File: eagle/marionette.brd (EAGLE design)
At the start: 139.7 x 76.2 mm, 227 parts, among them J17 MA02-1, J18 MA02-1, J19 MA02-1, J2 SWD, J20 MA02-1, J22 ZX62D-B-5P8, J6 MA03-2W, J8 MA04-2W, Q1 BSS84, U1 STM32F407, U10 LVM344, U12 AT24C04D, U13 CON_HIROSE_DM3D(MICROSD), U14 USB3320, U2 NCP705, U3 XCL206B, U4 AAT3221, U5 MAX3051ESA, U6 DAC124S085CIMM, U7 LVM344, U8 LVM344, U9 LVM344, X1 ABSO7, X2 NX3225SA

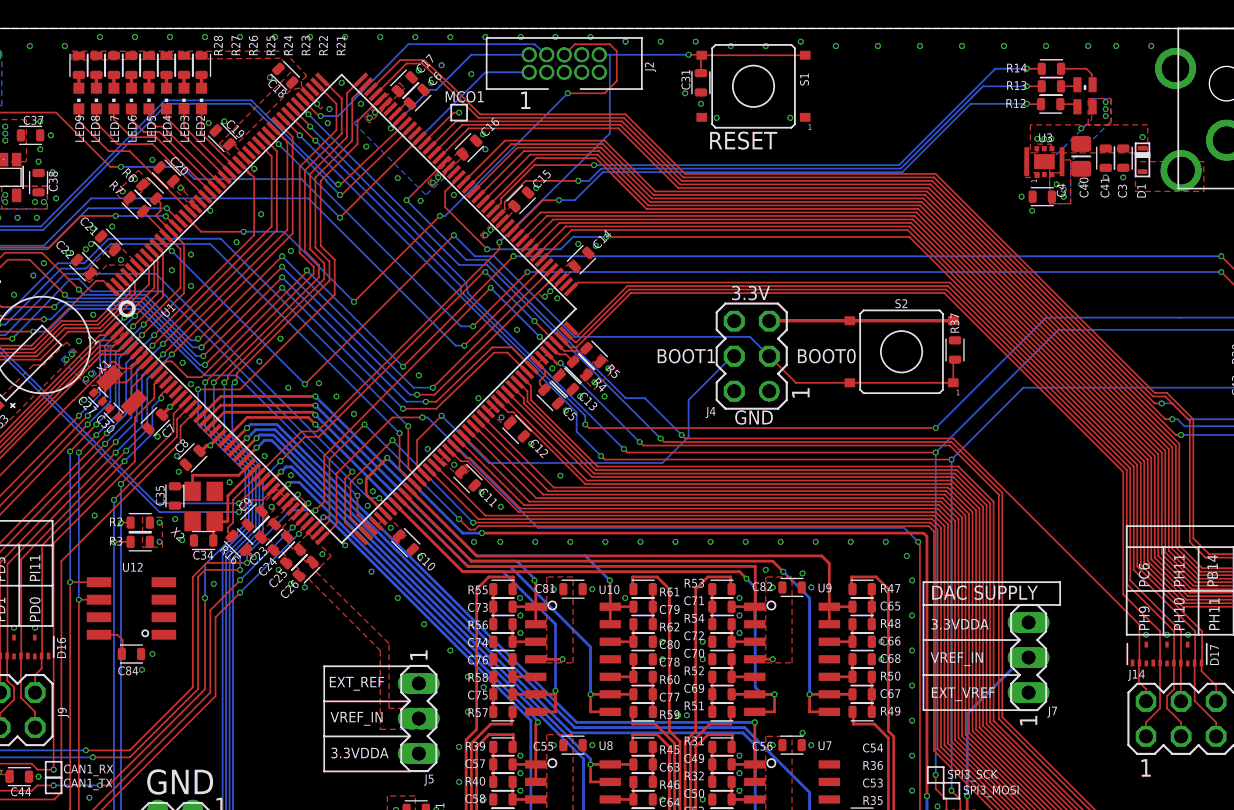
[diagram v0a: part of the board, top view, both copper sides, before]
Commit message: Added new 3.3V SPS and related LC components Changed Vin header to DAC from 3pin to 2pin
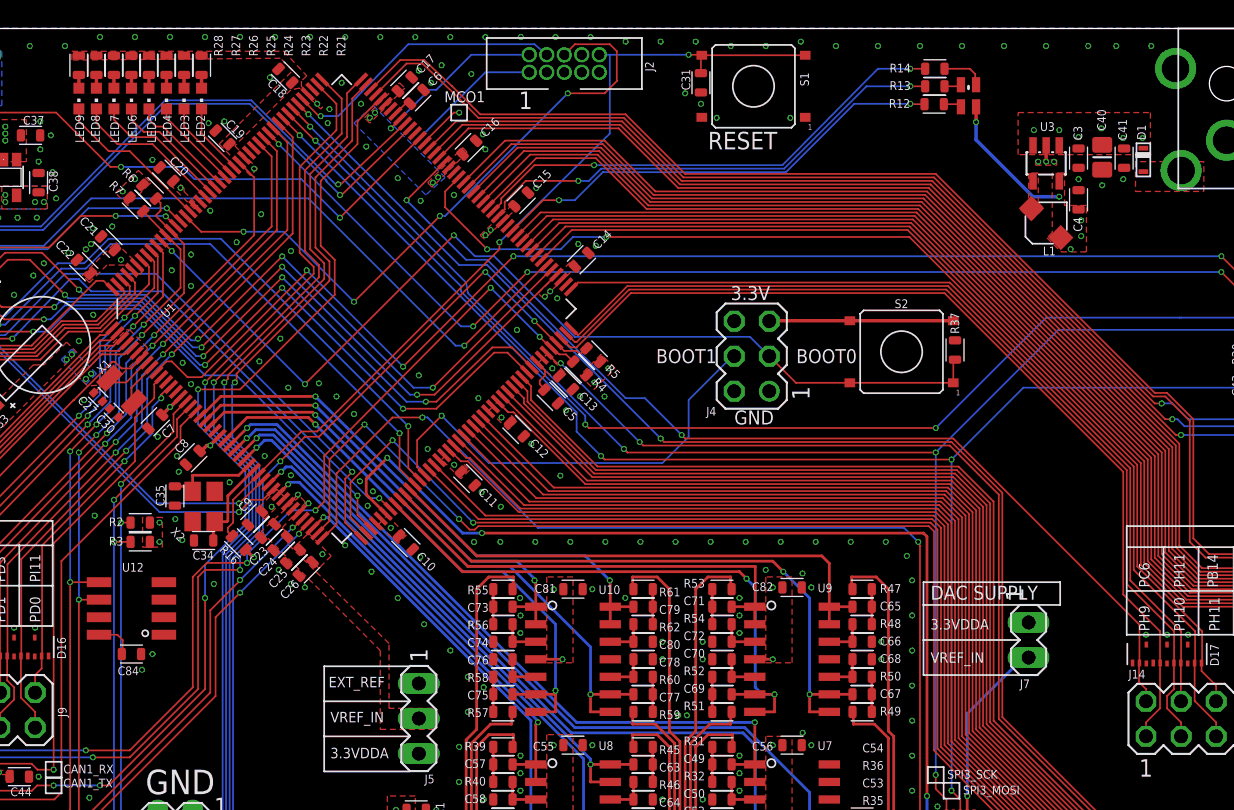
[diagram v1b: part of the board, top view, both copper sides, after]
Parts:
- added L1: 2.2uH, rcl_custom:CDRH2D14
- C1, C2, C23, C25, C37, C38, C41, C46: value 1uF, 10V -> 1uF
- C10, C12, C13, C14, C15, C16, C17, C18, C19, C20, C21, C24, C26, C31, C7, C8, C9: value 100nF, 10V -> .1uF
- C11: value 100nF, 10V -> .1uf
- C22: value 4.7uF, 10v -> 4.7uF
- C3: value 4.7uF, 10V -> 4.7uF
- C33: value EDLC -> 220mF
- C39, C4, C40, C45: value 10uF, 10V -> 10uF
- C47: value 0.1uF, 10V Low ESR -> 0.1uF
- C5, C6: value 2.2uF, 10V -> 2.2uF
- C55, C56, C81, C82: value (none) -> 1uF
- J7: value (none) -> MA02-1; device MA_HEADER:MA03-1 -> MA_HEADER:MA02-1
- U3: value XCL206B -> LM3671; device XCL206B:56-BCPGA -> LM3671:SOT23-5L
- moved LED1 8.45 mm to (97.2, 71.3)
- moved R13 8.45 mm to (94.8, 72.0)
- moved R14 8.45 mm to (94.8, 73.3)
- moved R12 8.45 mm to (94.8, 70.7)
- moved C3 3.24 mm to (105.2, 66.8)
- moved C4 2.64 mm to (105.2, 63.8), turned to 90 degrees
- moved C40 1.53 mm to (106.9, 66.9)
- moved C41 1.33 mm to (108.5, 66.8)
- moved J7 1.27 mm to (101.6, 31.9), turned to 270 degrees
- moved U3 0.18 mm to (102.9, 66.4), turned to 180 degrees
- moved D1 0.06 mm to (109.9, 66.7)
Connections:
- removed net N$5: U3.1, U3.7
- new net N$41: L1.2, U3.4
- net +3.3VDDA: now also J7.1; no longer J7.3
- net 3.3VDD: now also L1.1, U3.5; no longer U3.3, U3.8
- net GND: no longer U3.5, U3.9
- net VCC: now also U3.1, U3.3; no longer U3.4, U3.6
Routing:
- net 3.3VDD: track 32.7 -> 42.8 mm, vias 46 -> 45
- net PD13: track 42.2 -> 33.7 mm
- net PD14: track 43.8 -> 35.4 mm
- net PD15: track 44.2 -> 35.8 mm
- net GND: track 2.46 -> 3.63 mm, vias 414 -> 415
- added copper zone on layer 1, net N$41
- removed copper zone on layer 1, net N$5
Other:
- board text removed: "EXT_VREF"

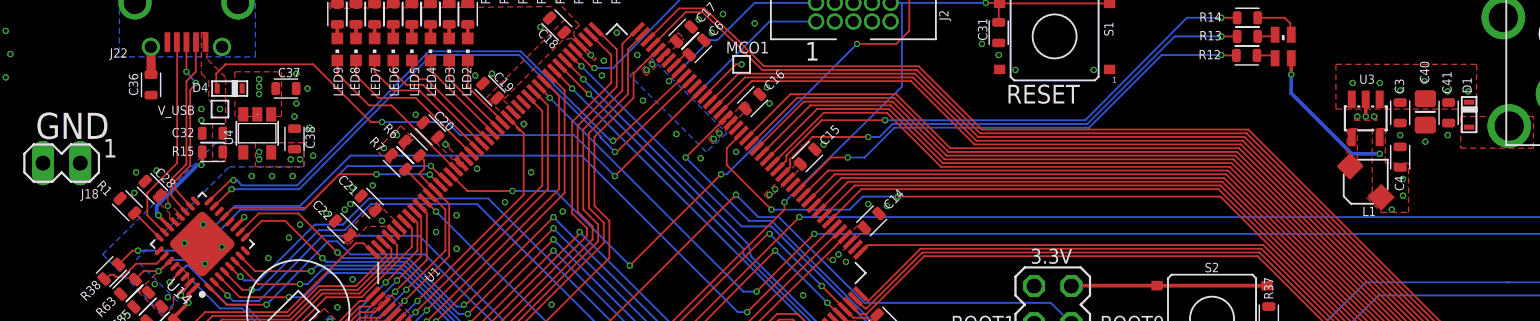
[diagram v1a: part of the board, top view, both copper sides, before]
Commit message: added 0805 10uF cap to 3.3sps.
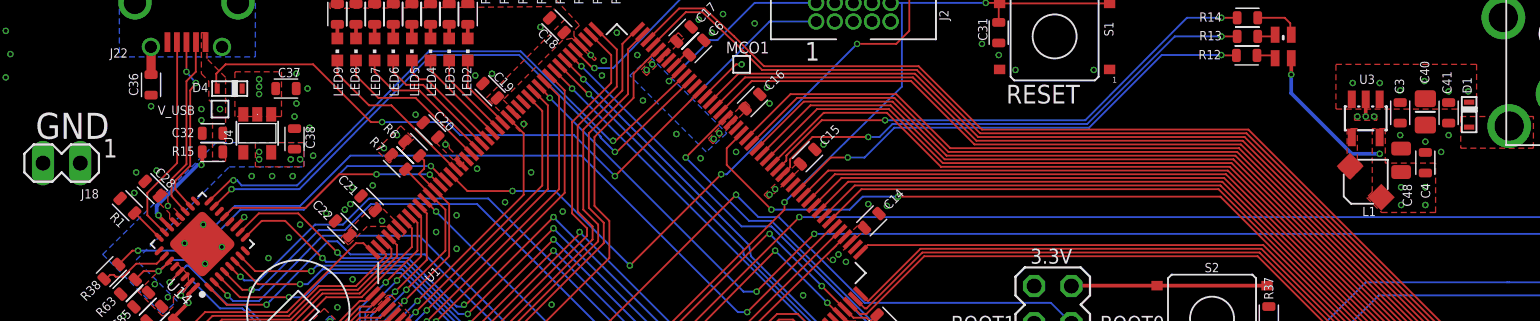
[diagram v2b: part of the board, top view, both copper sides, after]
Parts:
- added C48: 10uf, rcl_custom:.0805-C-NOSILK
- C4: value 10uF -> 1uf
- moved C4 1.76 mm to (106.9, 63.4)
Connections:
- net 3.3VDD: now also C48.1
- net GND: now also C48.2
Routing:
- net GND: vias 415 -> 417
- net 3.3VDD: vias 45 -> 46
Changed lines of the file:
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@@
 <attribute name="NAME" x="93.345" y="16.129" size="0.3" layer="33" ratio="15" rot="R270" align="center"/>
 </element>
-<element name="C4" library="rcl_custom" package=".0603-C" value="10uF" x="105.2195" y="63.7794" smashed="yes" rot="R90">
-<attribute name="NAME" x="105.4855" y="61.4713" size="0.635" layer="25" font="vector" ratio="20" rot="R90"/>
-<attribute name="NAME" x="105.2195" y="63.7794" size="0.3" layer="33" ratio="15" rot="R90" align="center"/>
+<element name="C4" library="rcl_custom" package=".0603-C" value="1uf" x="106.934" y="63.3984" smashed="yes" rot="R90">
+<attribute name="NAME" x="107.2635" y="60.9633" size="0.635" layer="25" font="vector" ratio="20" rot="R90"/>
+<attribute name="NAME" x="106.934" y="63.3984" size="0.3" layer="33" ratio="15" rot="R90" align="center"/>
 </element>
 <element name="C40" library="rcl_custom" package=".0805-B" value="10uF" x="106.934" y="66.8655" smashed="yes" rot="R270">
@@
 </element>
 <element name="R1" library="rcl_custom" package=".0603-C" value="8.06k" x="18.452196875" y="60.46740625" smashed="yes" rot="R135">
-<attribute name="NAME" x="17.497640625" y="61.514875" size="0.635" layer="25" font="vector" ratio="20" rot="R135"/>
+<attribute name="NAME" x="18.386640625" y="59.355875" size="0.635" layer="25" font="vector" ratio="20" rot="R135"/>
 <attribute name="NAME" x="18.452196875" y="60.46740625" size="0.3" layer="33" ratio="15" rot="R135" align="center"/>
 </element>
@@
 <attribute name="VALUE" x="98.679" y="34.417" size="1.27" layer="27" ratio="10" rot="R270"/>
 </element>
+<element name="C48" library="rcl_custom" package=".0805-C-NOSILK" value="10uf" x="105.283" y="63.5635" smashed="yes" rot="R90">
+<attribute name="NAME" x="106.0205" y="60.4085" size="0.635" layer="25" font="vector" ratio="20" rot="R90"/>
+<attribute name="VALUE" x="106.933" y="62.3135" size="0.8" layer="27" font="vector" ratio="15" rot="R90"/>
+<attribute name="NAME" x="105.283" y="63.5635" size="0.4" layer="33" ratio="15" rot="R90" align="center"/>
+</element>
 </elements>
 <signals>
@@
 <contactref element="U3" pad="2"/>
 <contactref element="C3" pad="2"/>
-<contactref element="C4" pad="2"/>
 <via x="103.4415" y="66.548" extent="1-16" drill="0.254"/>
 <via x="102.87" y="66.548" extent="1-16" drill="0.254"/>
@@
 <via x="105.2195" y="65.278" extent="1-16" drill="0.254"/>
 <via x="106.934" y="64.8335" extent="1-16" drill="0.254"/>
-<via x="108.458" y="65.278" extent="1-16" drill="0.254"/>
+<via x="108.5215" y="65.278" extent="1-16" drill="0.254"/>
 <polygon width="0.127" layer="1" isolate="0.2032" thermals="no" rank="2">
 <vertex x="103.632" y="66.675"/>
@@
 </polygon>
 <wire x1="102.87" y1="67.721" x2="102.87" y2="66.548" width="0.254" layer="1"/>
+<via x="20.066" y="67.2465" extent="1-16" drill="0.254"/>
+<contactref element="C48" pad="2"/>
+<contactref element="C4" pad="2"/>
+<via x="108.0135" y="64.135" extent="1-16" drill="0.254"/>
 <wire x1="22.352" y1="57.912" x2="23.553984375" y2="57.8530125" width="0" layer="19" extent="1-1"/>
 </signal>
@@
 <via x="103.8225" y="68.834" extent="1-16" drill="0.254"/>
 <via x="106.8705" y="68.961" extent="1-16" drill="0.254"/>
-<via x="108.458" y="68.2625" extent="1-16" drill="0.254"/>
+<via x="108.5215" y="68.2625" extent="1-16" drill="0.254"/>
 <via x="109.855" y="68.2625" extent="1-16" drill="0.254"/>
 </signal>
@@
 <contactref element="C4" pad="1"/>
 <polygon width="0.127" layer="1" isolate="0.2032" thermals="no">
-<vertex x="104.0765" y="65.7225"/>
+<vertex x="104.2035" y="65.7225"/>
 <vertex x="103.3145" y="65.7225"/>
-<vertex x="103.3145" y="61.468"/>
 <vertex x="103.3145" y="61.4045"/>
 <vertex x="102.9335" y="61.0235"/>
 <vertex x="103.9495" y="60.0075"/>
-<vertex x="105.791" y="60.0075"/>
-<vertex x="105.791" y="63.373"/>
+<vertex x="107.6325" y="60.0075"/>
+<vertex x="107.6325" y="63.373"/>
 <vertex x="104.2035" y="63.373"/>
-<vertex x="104.2035" y="65.7225"/>
 </polygon>
-<via x="104.648" y="60.198" extent="1-16" drill="0.254"/>
-<via x="105.41" y="61.1505" extent="1-16" drill="0.254"/>
-<via x="105.41" y="62.2935" extent="1-16" drill="0.254"/>
+<via x="105.283" y="60.5155" extent="1-16" drill="0.254"/>
+<via x="106.934" y="61.722" extent="1-16" drill="0.254"/>
+<via x="105.283" y="61.722" extent="1-16" drill="0.254"/>
 <via x="97.79" y="69.4055" extent="1-16" drill="0.254"/>
 <via x="103.8225" y="64.008" extent="1-16" drill="0.254"/>
@@
 <wire x1="97.7939" y1="70.5232" x2="97.7939" y2="69.4094" width="0.254" layer="1"/>
 <wire x1="97.7939" y1="69.4094" x2="97.79" y2="69.4055" width="0.254" layer="1"/>
+<contactref element="C48" pad="1"/>
+<via x="106.934" y="60.5155" extent="1-16" drill="0.254"/>
 </signal>
 <signal name="PD6">

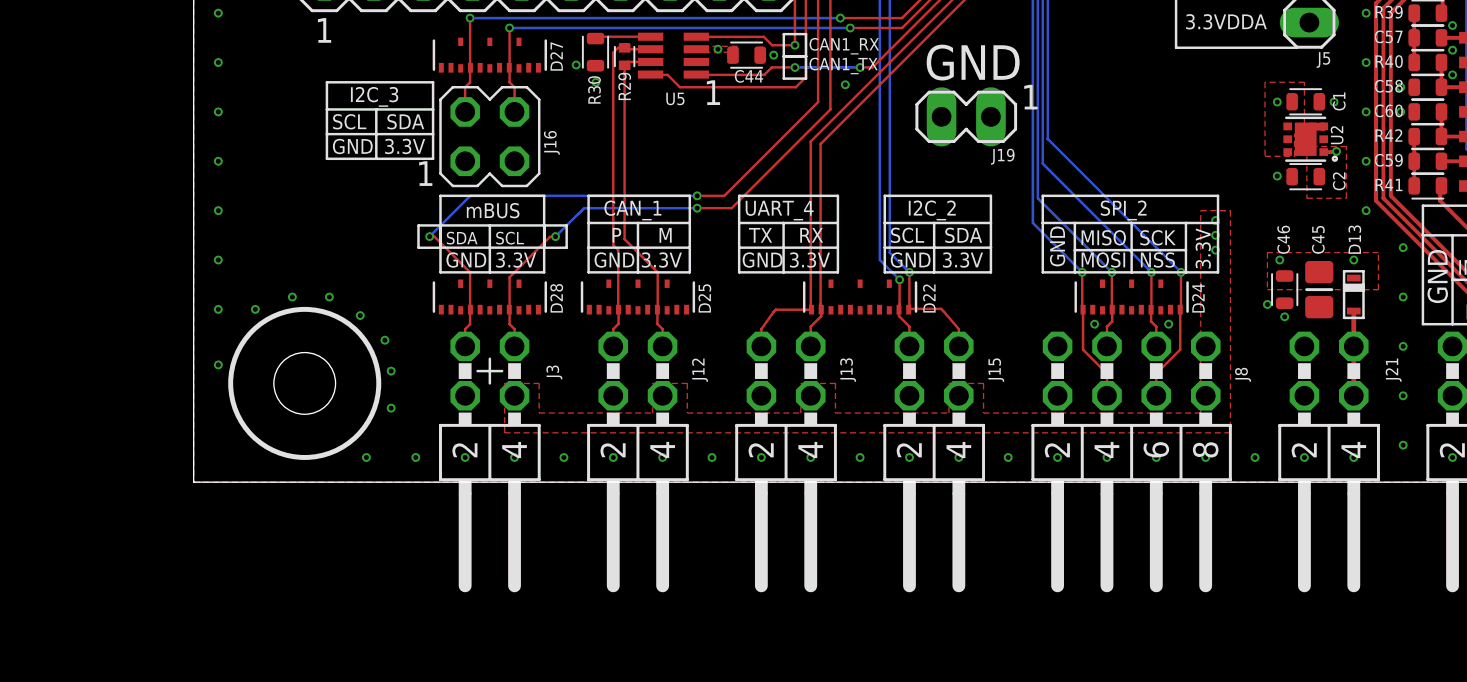
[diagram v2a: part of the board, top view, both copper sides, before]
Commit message: Added new 1.8V/3.3V LDO and associated bypass caps to schematic
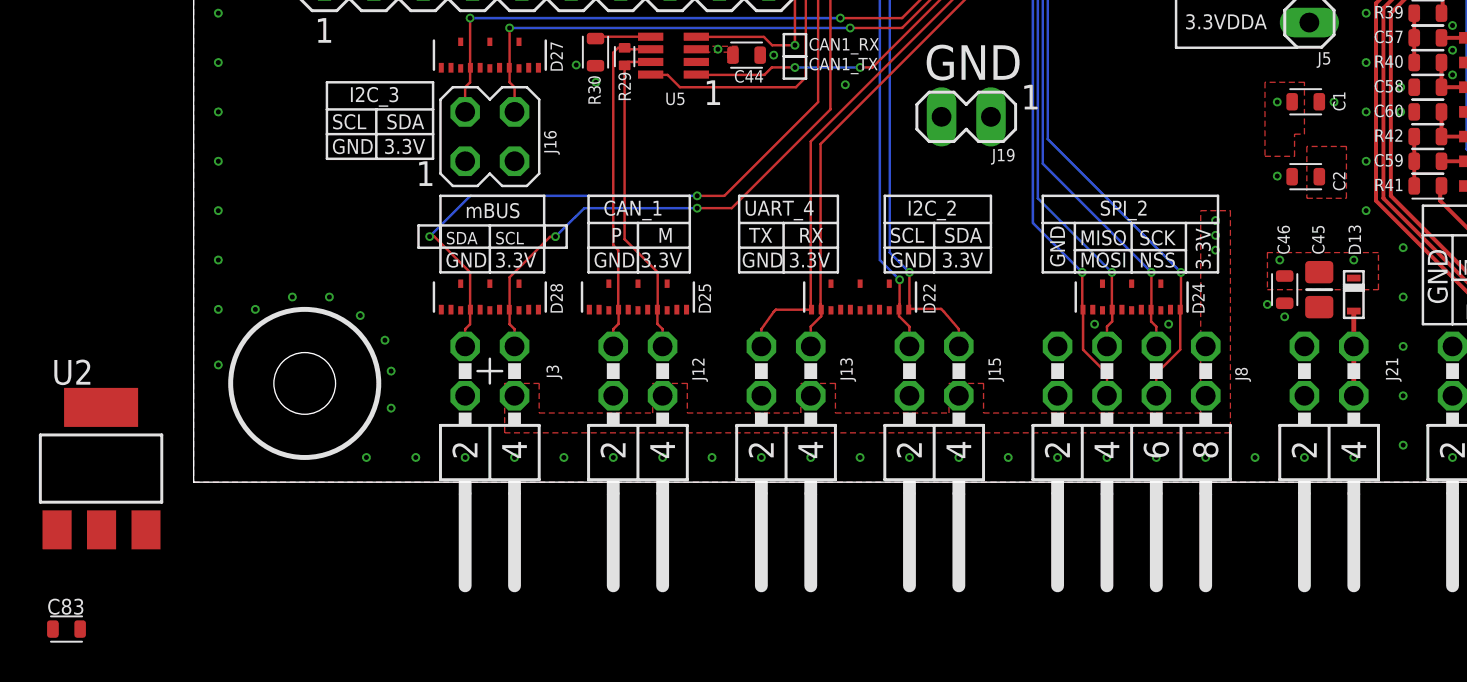
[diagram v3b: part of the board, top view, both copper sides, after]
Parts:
- added C83: 0.1uF, rcl_custom:.0603-C
- C38: value 1uF -> 2.2uF
- U2: value NCP705 -> TC1262; device NCP705:WDFN6 -> TC1262:SOT223
- U4: value AAT3221 -> LK112; device AAT3221:SOT23-5 -> LK112:SOT23-5
- moved U2 64.3 mm to (-4.76, 0.70), turned to 0 degrees
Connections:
- new net N$5: C83.1, U4.3
- net +1.8V: now also U4.4; no longer U4.5
- net +3.3VDDA: now also U2.3; no longer U2.1
- net 3.3VDD: now also C1.1, C37.1, U2.1, U4.1, U4.5
- net GND: now also C83.2, U2.2, U2.4; no longer U2.3, U2.GND
- net VCC: no longer C1.1, C37.1, U2.4, U2.6, U4.1, U4.3
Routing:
- net GND: track 3.63 -> 2.17 mm
- net +3.3VDDA: track 7.35 -> 6.67 mm, vias 13 -> 12

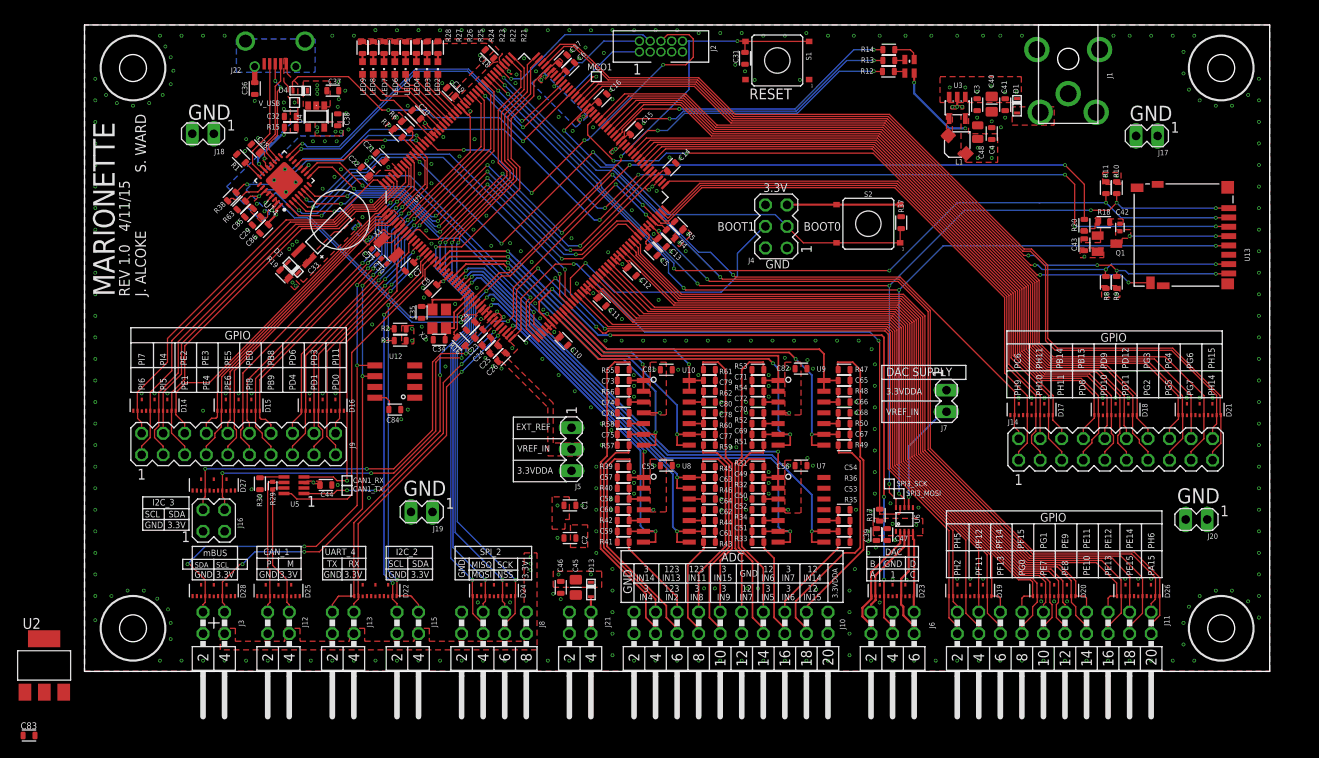
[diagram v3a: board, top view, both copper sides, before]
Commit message: Added replacement 1.8V/3.3V LDO and associated bypass caps
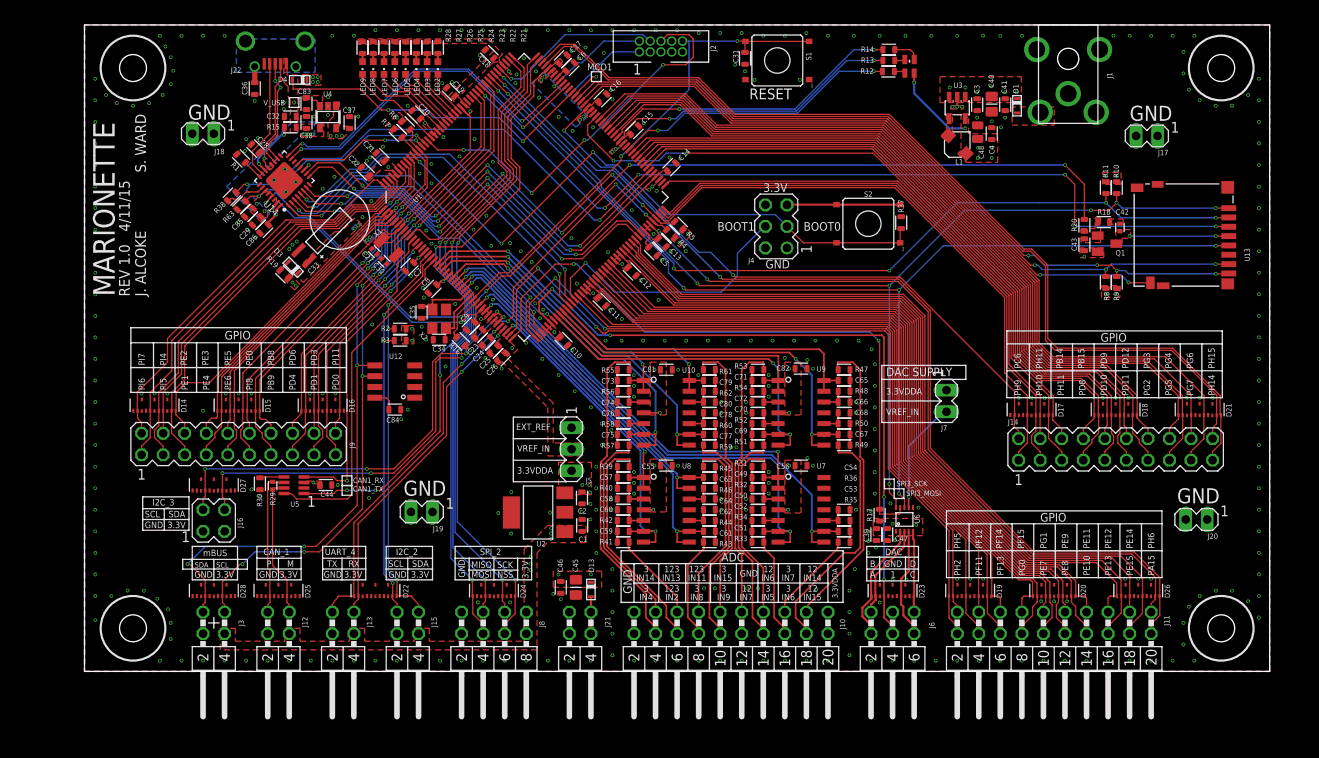
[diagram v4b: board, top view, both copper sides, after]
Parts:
- moved C83 81.3 mm to (26.2, 66.9), turned to 270 degrees
- moved U2 61.0 mm to (53.5, 18.7), turned to 90 degrees
- moved C2 4.94 mm to (58.6, 20.4), turned to 270 degrees
- moved C37 4.25 mm to (31.2, 64.7), turned to 90 degrees
- moved C38 3.70 mm to (26.2, 64.7)
- moved C1 2.77 mm to (58.7, 17.2), turned to 90 degrees
- moved U4 1.40 mm to (28.7, 65.3)
- moved D4 1.27 mm to (25.4, 69.7)
- moved V_USB 0.06 mm to (24.7, 67.1)
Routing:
- net V_USB: track 39.8 -> 38.9 mm
- net 3.3VDD: vias 46 -> 52
- net +3.3VDDA: vias 12 -> 15
- added copper zone on layer 1, net N$5
